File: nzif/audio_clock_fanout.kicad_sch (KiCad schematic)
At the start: 1 part, among them U15 AD9508BCPZ

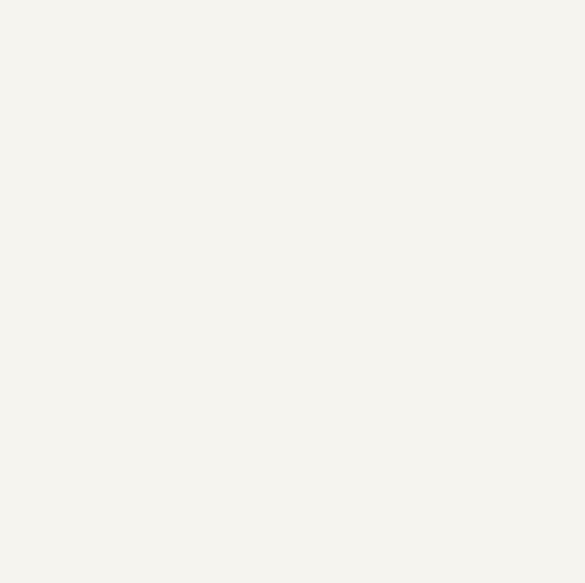
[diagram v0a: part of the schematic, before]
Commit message: add klc compliant mixer
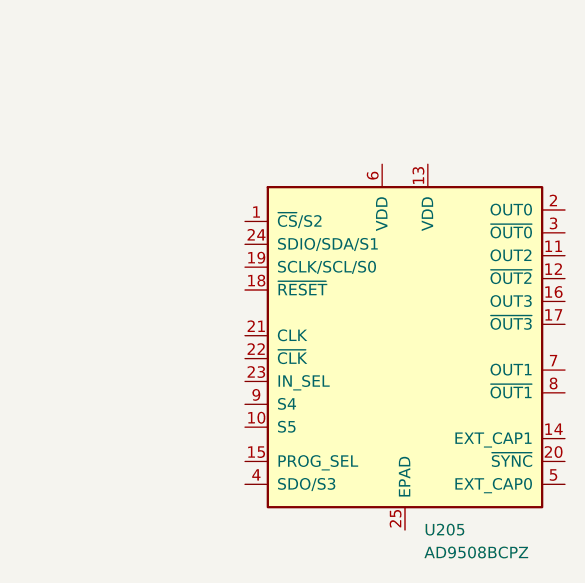
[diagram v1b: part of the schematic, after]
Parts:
- added U205: AD9508BCPZ, CP_24_7_ADI, symbol nzif_radio_symbol_library:AD9508BCPZ
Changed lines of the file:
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@@
+	)
+	(symbol
+		(lib_id "nzif_radio_symbol_library:AD9508BCPZ")
+		(at 181.61 154.94 0)
+		(unit 1)
+		(exclude_from_sim no)
+		(in_bom yes)
+		(on_board yes)
+		(dnp no)
+		(fields_autoplaced yes)
+		(property "Reference" "U205"
+			(at 183.7533 175.26 0)
+			(effects
+				(font
+					(size 1.27 1.27)
+				)
+				(justify left)
+			)
+		)
+		(property "Value" "AD9508BCPZ"
+			(at 183.7533 177.8 0)
+			(effects
+				(font
+					(size 1.27 1.27)
+				)
+				(justify left)
+			)
+		)
+		(property "Footprint" "CP_24_7_ADI"
+			(at 181.61 154.94 0)
+			(effects
+				(font
+					(size 1.27 1.27)
+					(italic yes)
+				)
+				(hide yes)
+			)
+		)
+		(property "Datasheet" "https://www.analog.com/media/en/technical-documentation/data-sheets/AD9508.pdf"
+			(at 181.61 154.94 0)
+			(effects
+				(font
+					(size 1.27 1.27)
+					(italic yes)
+				)
+				(hide yes)
+			)
+		)
+		(property "Description" "4-Channel Clock Fanout Buffer with Dividers, LFCSP-24"
+			(at 181.61 154.94 0)
+			(effects
+				(font
+					(size 1.27 1.27)
+				)
+				(hide yes)
+			)
+		)
+		(pin "18"
+		)
+		(pin "8"
+		)
+		(pin "23"
+		)
+		(pin "6"
+		)
+		(pin "4"
+		)
+		(pin "11"
+		)
+		(pin "7"
+		)
+		(pin "1"
+		)
+		(pin "21"
+		)
+		(pin "17"
+		)
+		(pin "10"
+		)
+		(pin "16"
+		)
+		(pin "2"
+		)
+		(pin "14"
+		)
+		(pin "20"
+		)
+		(pin "22"
+		)
+		(pin "24"
+		)
+		(pin "25"
+		)
+		(pin "12"
+		)
+		(pin "9"
+		)
+		(pin "15"
+		)
+		(pin "13"
+		)
+		(pin "19"
+		)
+		(pin "3"
+		)
+		(pin "5"
+		)
+		(instances
+			(project ""
+				(path "/fe42ca2f-2bb8-4d5a-9e84-807788ed632f/ea1efef5-9a17-4347-a6bd-c783dedda463"
+					(reference "U205")
+					(unit 1)
+				)
+			)
+		)
 	)
 	(symbol
